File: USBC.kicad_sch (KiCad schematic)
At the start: 1 part, among them J4 USB_C_Receptacle

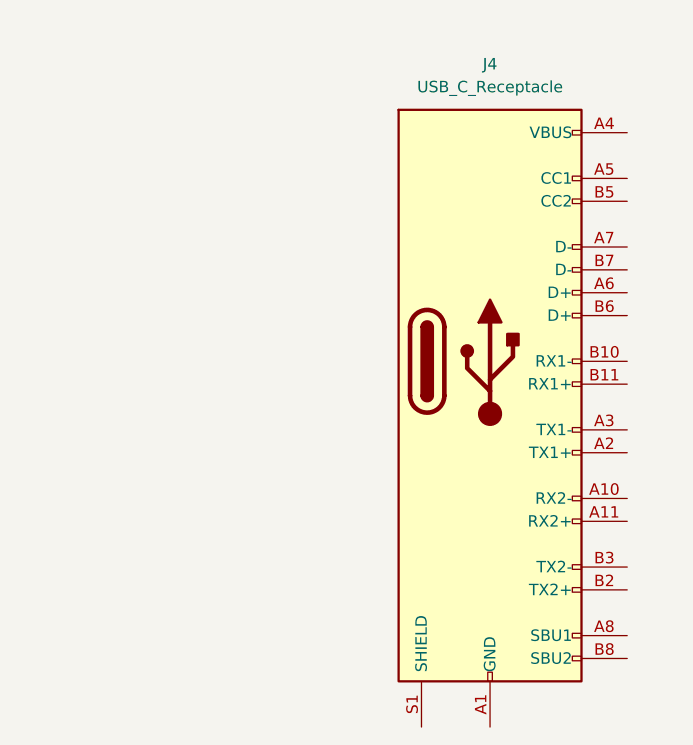
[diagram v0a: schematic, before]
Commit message: Fix: fixed usb receptacle
Changed footprint and wired up usb C
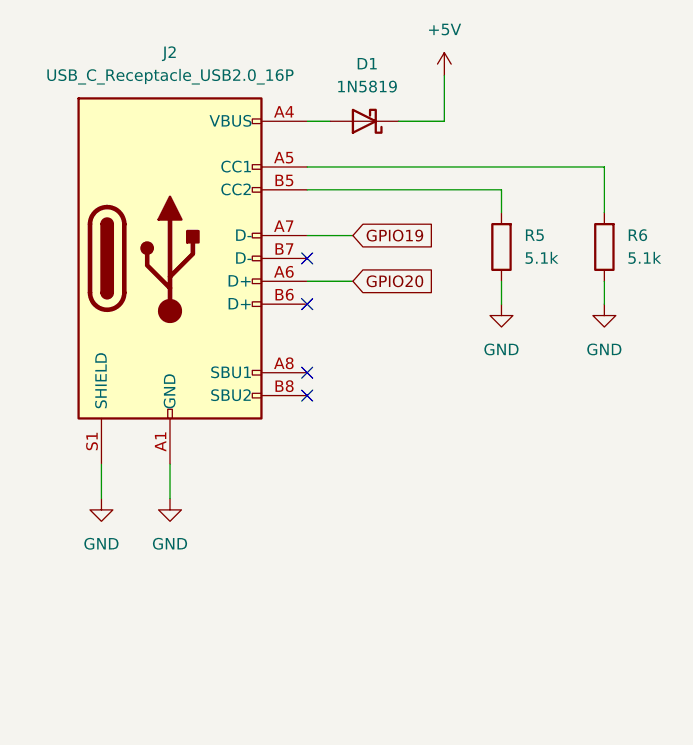
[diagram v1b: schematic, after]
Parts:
- removed J4: USB_C_Receptacle, symbol Connector:USB_C_Receptacle
- added D1: 1N5819, Diode_THT:D_DO-41_SOD81_P10.16mm_Horizontal, symbol Diode:1N5819
- added J2: USB_C_Receptacle_USB2.0_16P, symbol Connector:USB_C_Receptacle_USB2.0_16P
- added R5, R6: 5.1k, Resistor_SMD:R_0603_1608Metric_Pad0.98x0.95mm_HandSolder, symbol Device:R
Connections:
- new net: J2.A5 (CC1), R6.2
- new net: J2.B5 (CC2), R5.2
- new net: D1.2 (A), J2.A4 (VBUS), J2.A9 (VBUS), J2.B4 (VBUS), J2.B9 (VBUS)
- new net +5V: D1.1 (K)
- new net GND: J2.A1 (GND), J2.A12 (GND), J2.B1 (GND), J2.B12 (GND), J2.S1 (SHIELD), R5.1, R6.1
- new net GPIO19: J2.A7 (D-)
- new net GPIO20: J2.A6 (D+)
- no-connect marks 0 -> 4

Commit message: updated schematic
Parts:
- removed D1: 1N5819, Diode_THT:D_DO-41_SOD81_P10.16mm_Horizontal, symbol Diode:1N5819
- removed J2: USB_C_Receptacle_USB2.0_16P, symbol Connector:USB_C_Receptacle_USB2.0_16P
- removed R5, R6: 5.1k, Resistor_SMD:R_0603_1608Metric_Pad0.98x0.95mm_HandSolder, symbol Device:R
- added J4: USB_C_Receptacle, symbol Connector:USB_C_Receptacle
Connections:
- new net: J4.A1 (GND), J4.A12 (GND), J4.B1 (GND), J4.B12 (GND)
- new net: J4.A4 (VBUS), J4.A9 (VBUS), J4.B4 (VBUS), J4.B9 (VBUS)
- no-connect marks 4 -> 0
